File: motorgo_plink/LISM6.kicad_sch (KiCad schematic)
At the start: 20 parts, among them J23 Conn_01x06_Pin, U10 LIS3MDLTR, U11 LSM6DS3TR

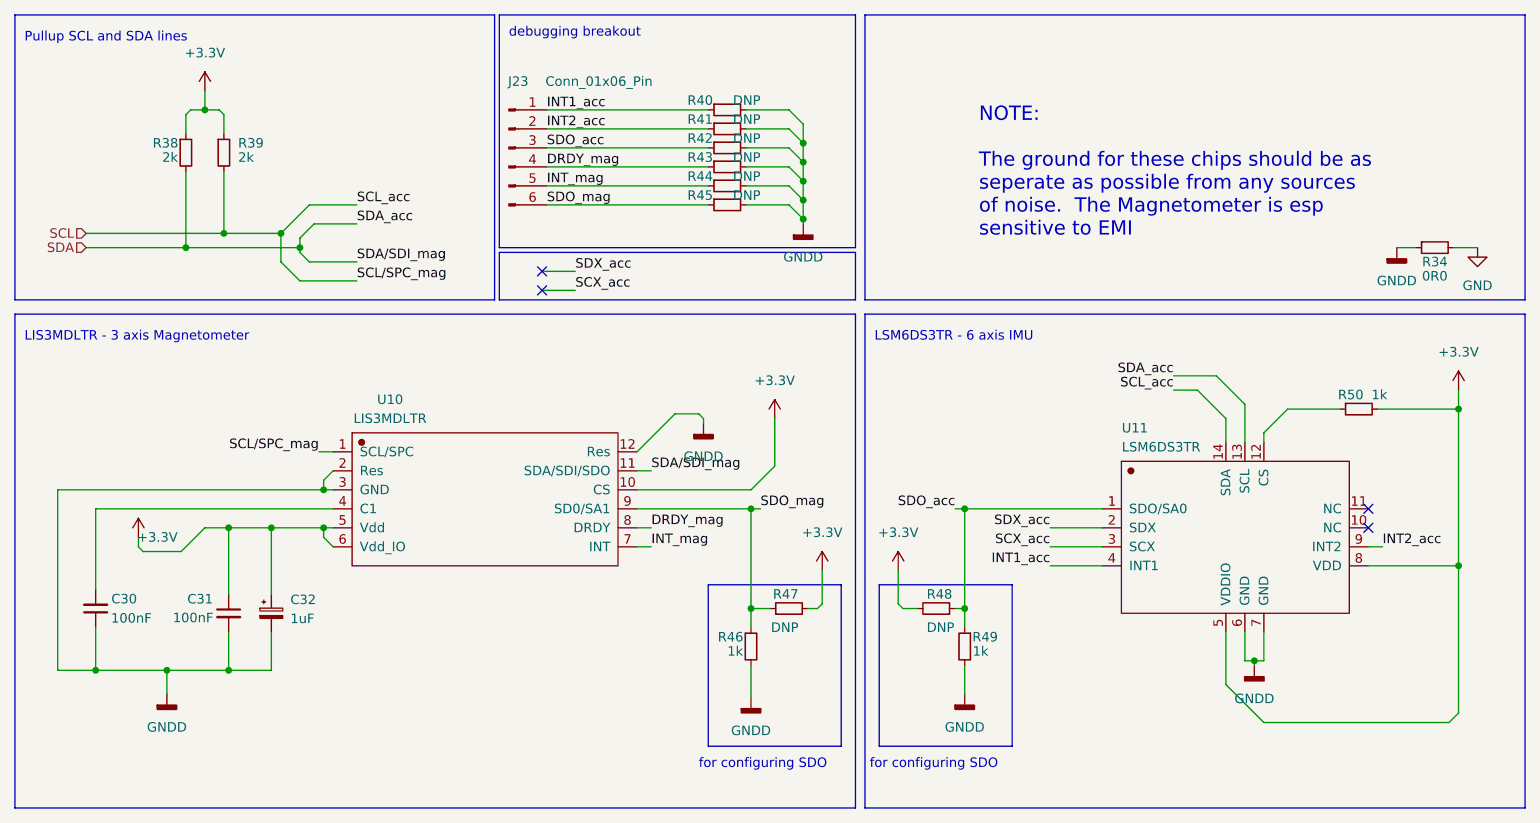
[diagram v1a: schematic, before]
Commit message: wip culling schematics and removing tracks
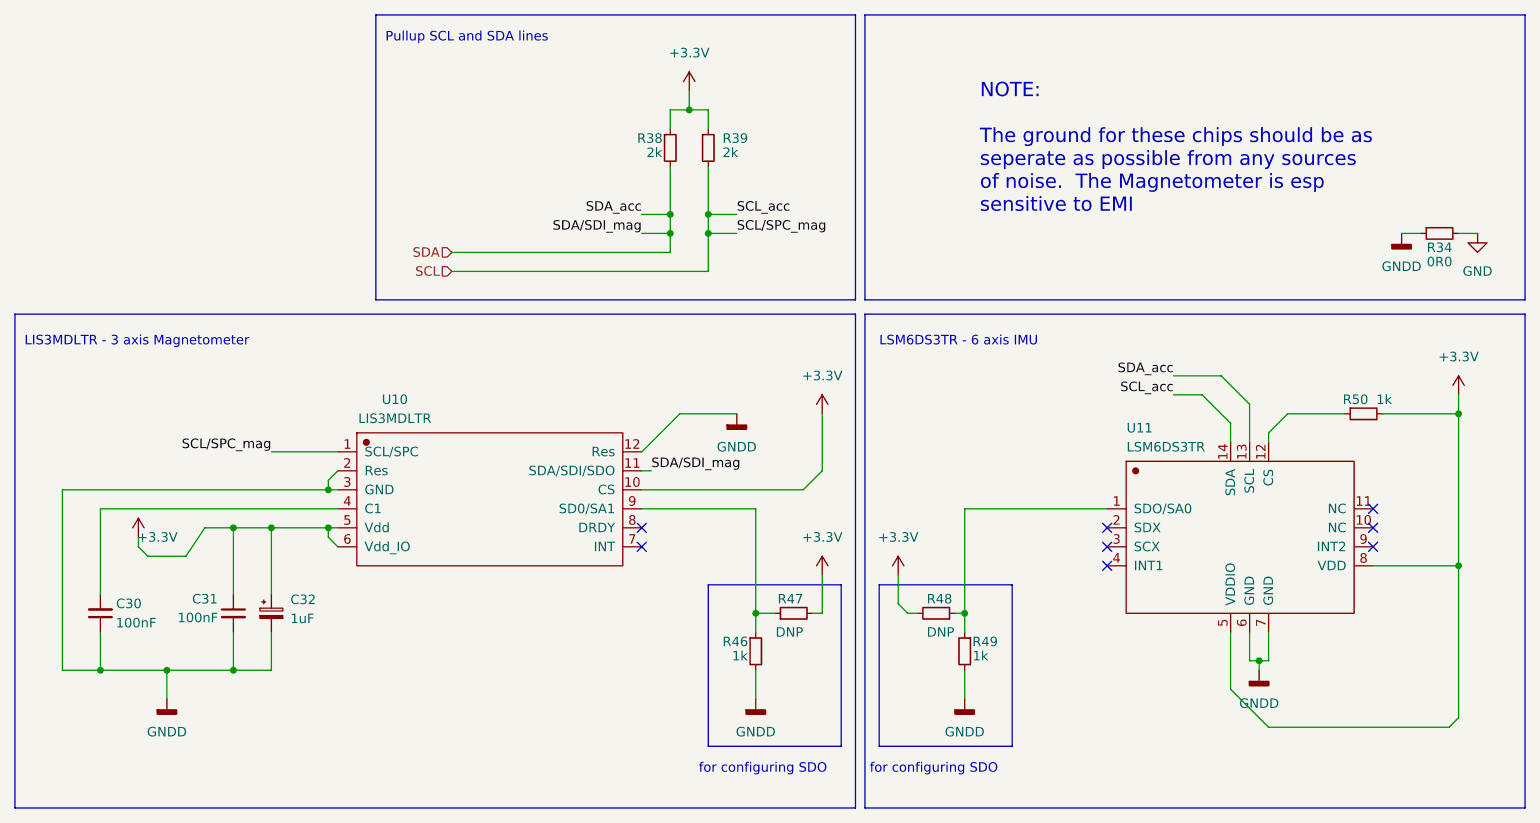
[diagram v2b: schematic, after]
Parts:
- removed J23: Conn_01x06_Pin, Connector_PinHeader_1.00mm:PinHeader_1x06_P1.00mm_Vertical, symbol Connector:Conn_01x06_Pin
- removed R40, R41, R42, R43, R44, R45: DNP, Resistor_SMD:R_0402_1005Metric, symbol Device:R_Small
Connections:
- net DRDY_mag: no longer names the net of U10.8 (DRDY)
- net INT1_acc: no longer names the net of U11.4 (INT1)
- net INT2_acc: no longer names the net of U11.9 (INT2)
- net INT_mag: no longer names the net of U10.7 (INT)
- net SCX_acc: no longer names the net of U11.3 (SCX)
- net SDO_acc: no longer names the net of R48.1, R49.1, U11.1 (SDO/SA0)
- net SDO_mag: no longer names the net of R46.1, R47.1, U10.9 (SD0/SA1)
- net SDX_acc: no longer names the net of U11.2 (SDX)
- no-connect marks 4 -> 8
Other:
- note removed: "debugging breakout"
- moved on the sheet: C30, C31, R34, R38, R39, R46, R47, R48, R49, R50, U10, U11

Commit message: wip layout work begun, board dimensions finalized
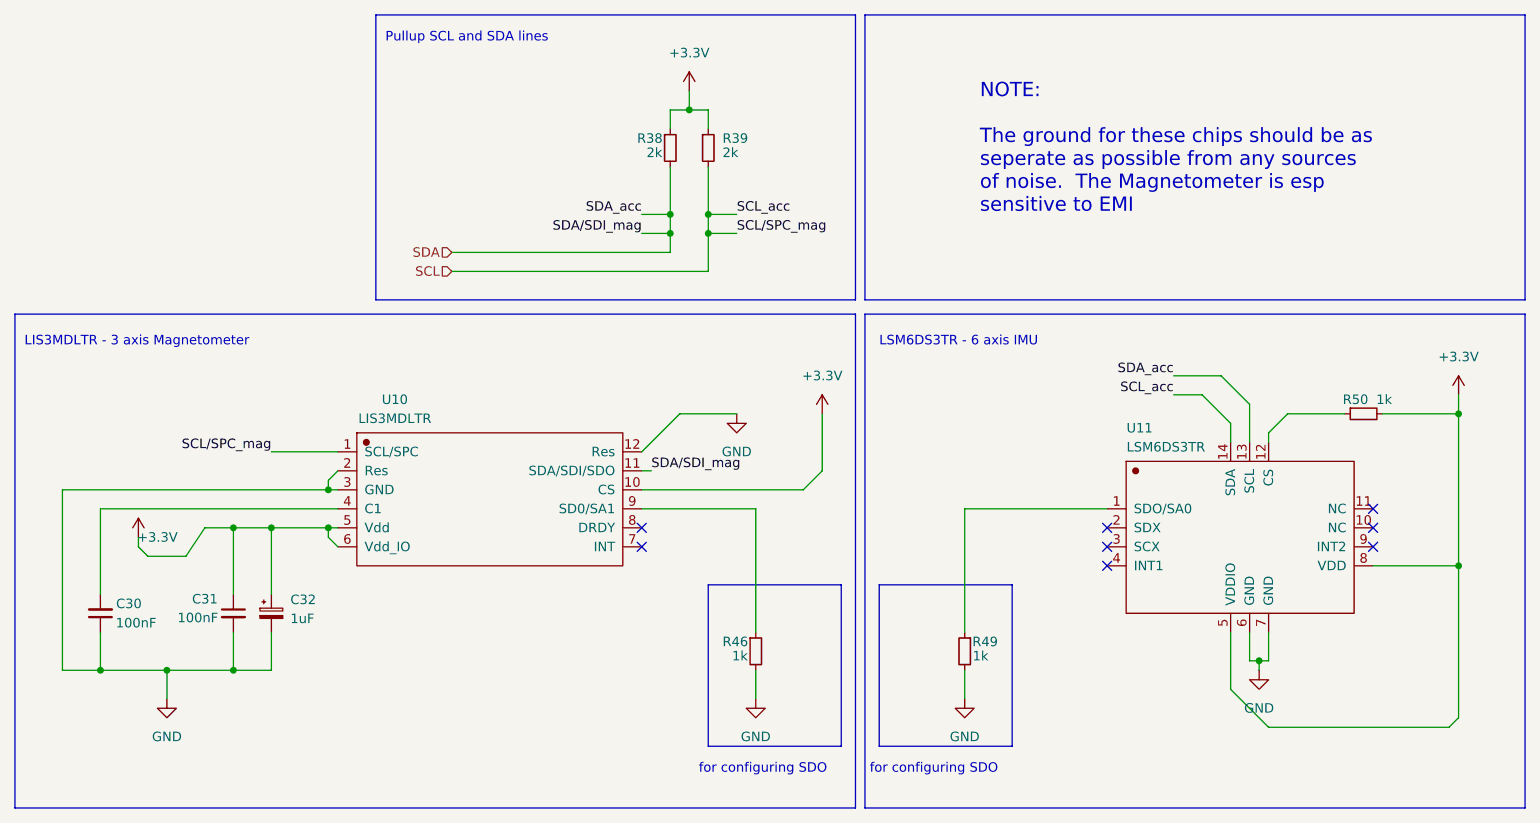
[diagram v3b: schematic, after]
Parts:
- removed R34: 0R0, Resistor_SMD:R_0603_1608Metric, symbol Device:R_Small
- removed R47, R48: DNP, Resistor_SMD:R_0402_1005Metric, symbol Device:R_Small
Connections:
- net GNDD is gone; now on net GND: C30.1, C31.2, C32.2, R46.2, R49.2, U10.12 (Res), U10.2 (Res), U10.3 (GND), U11.6 (GND), U11.7 (GND)

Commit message: production files and all edits for final send off of v1.0
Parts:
- R46, R49, R50: LCSC_Part_Number C2906899 -> C11702
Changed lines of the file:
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@@
 			)
 		)
-		(property "LCSC_Part_Number" "C2906899"
+		(property "LCSC_Part_Number" "C11702"
 			(at 175.26 124.46 0)
 			(effects
@@
 			)
 		)
-		(property "LCSC_Part_Number" "C2906899"
+		(property "LCSC_Part_Number" "C11702"
 			(at 147.32 124.46 0)
 			(effects
@@
 			)
 		)
-		(property "LCSC_Part_Number" "C2906899"
+		(property "LCSC_Part_Number" "C11702"
 			(at 228.6 92.71 0)
 			(effects

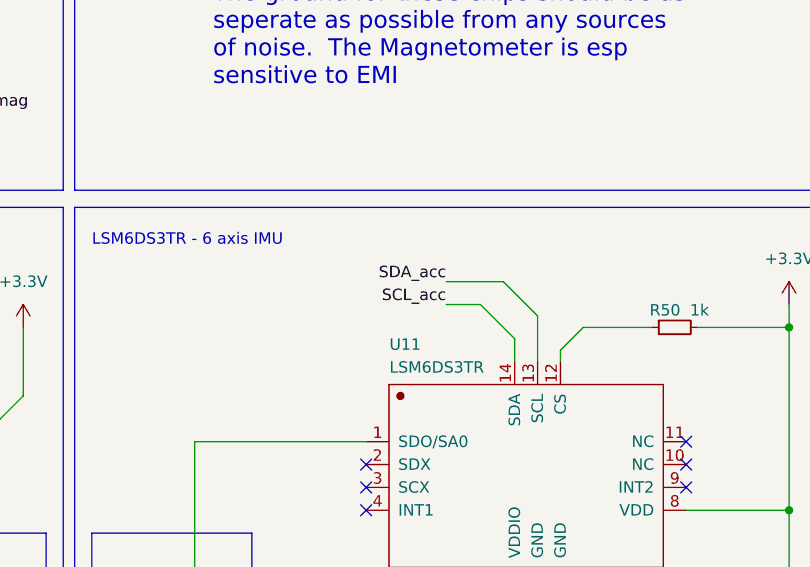
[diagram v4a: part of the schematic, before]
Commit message: updated schematic to fix IMU i2c mismatch, silkscreen readability, schottky backpower diode, and added RC Servo pins
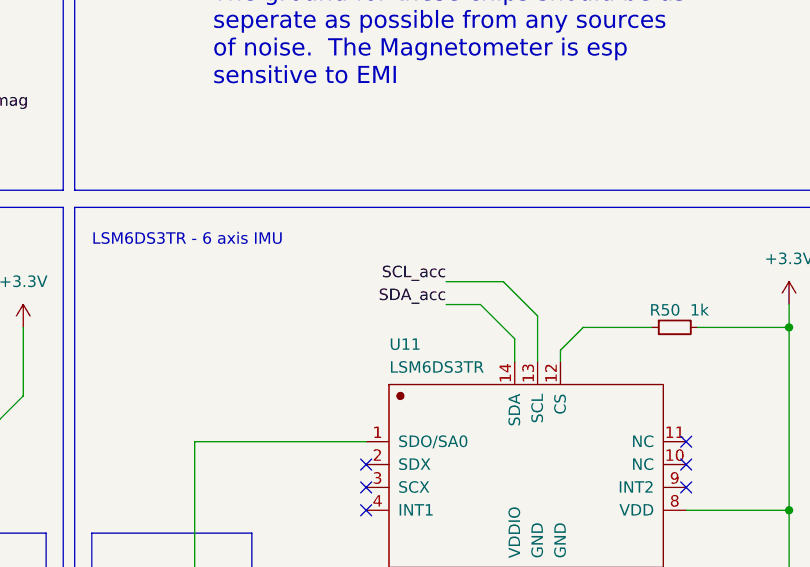
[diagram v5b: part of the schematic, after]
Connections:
- net SCL: now also U11.13 (SCL); no longer U11.14 (SDA)
- net SDA: now also U11.14 (SDA); no longer U11.13 (SCL)
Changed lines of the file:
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@@
 		)
 	)
-	(label "SDA_acc"
+	(label "SCL_acc"
 		(at 203.2 87.63 180)
 		(fields_autoplaced yes)
@@
 			)
 			(justify left bottom)
+		)
+	)
+	(label "SDA_acc"
+		(at 203.2 90.17 180)
+		(fields_autoplaced yes)
+		(effects
+			(font
+				(size 1.27 1.27)
+			)
+			(justify right bottom)
 		)
 	)
@@
 		)
 	)
-	(label "SCL_acc"
-		(at 203.2 90.17 180)
-		(fields_autoplaced yes)
-		(effects
-			(font
-				(size 1.27 1.27)
-			)
-			(justify right bottom)
-		)
-	)
